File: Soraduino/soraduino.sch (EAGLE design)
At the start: 1 part, among them IC1 ATMEGA168-AU

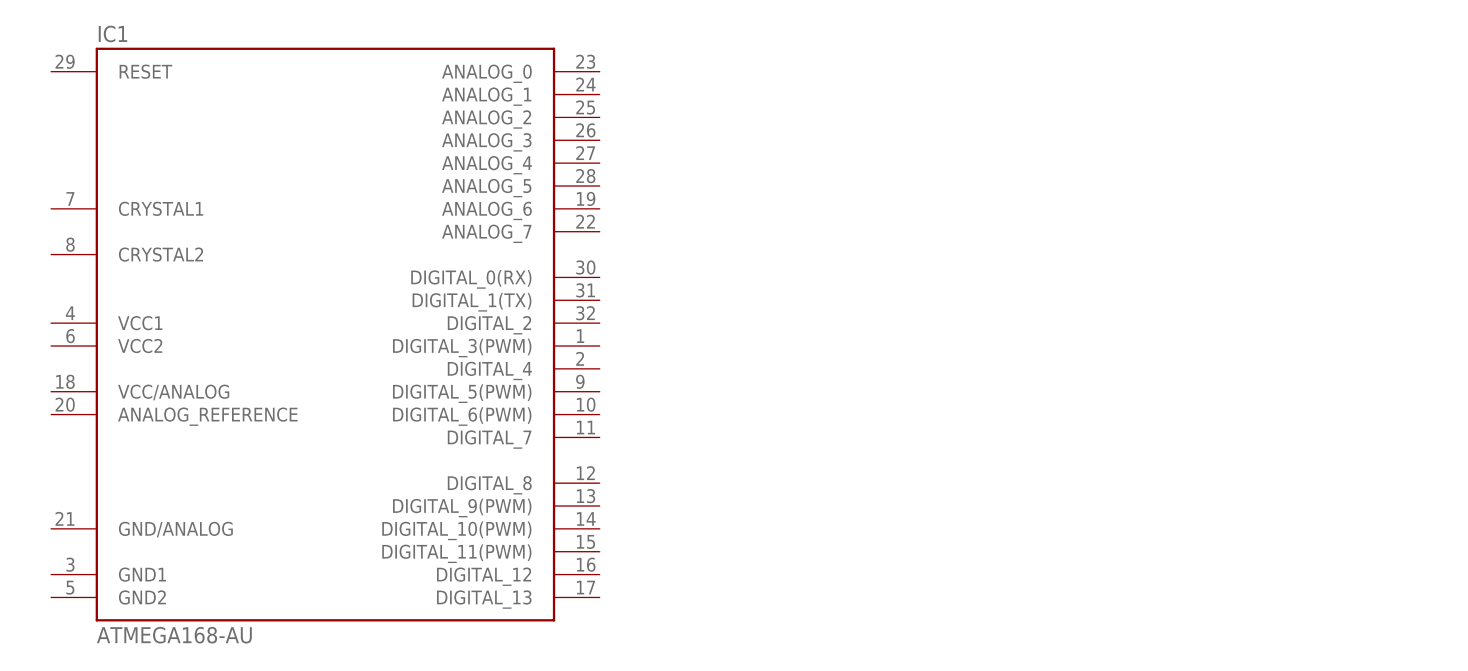
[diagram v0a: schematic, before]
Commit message: crystal設置
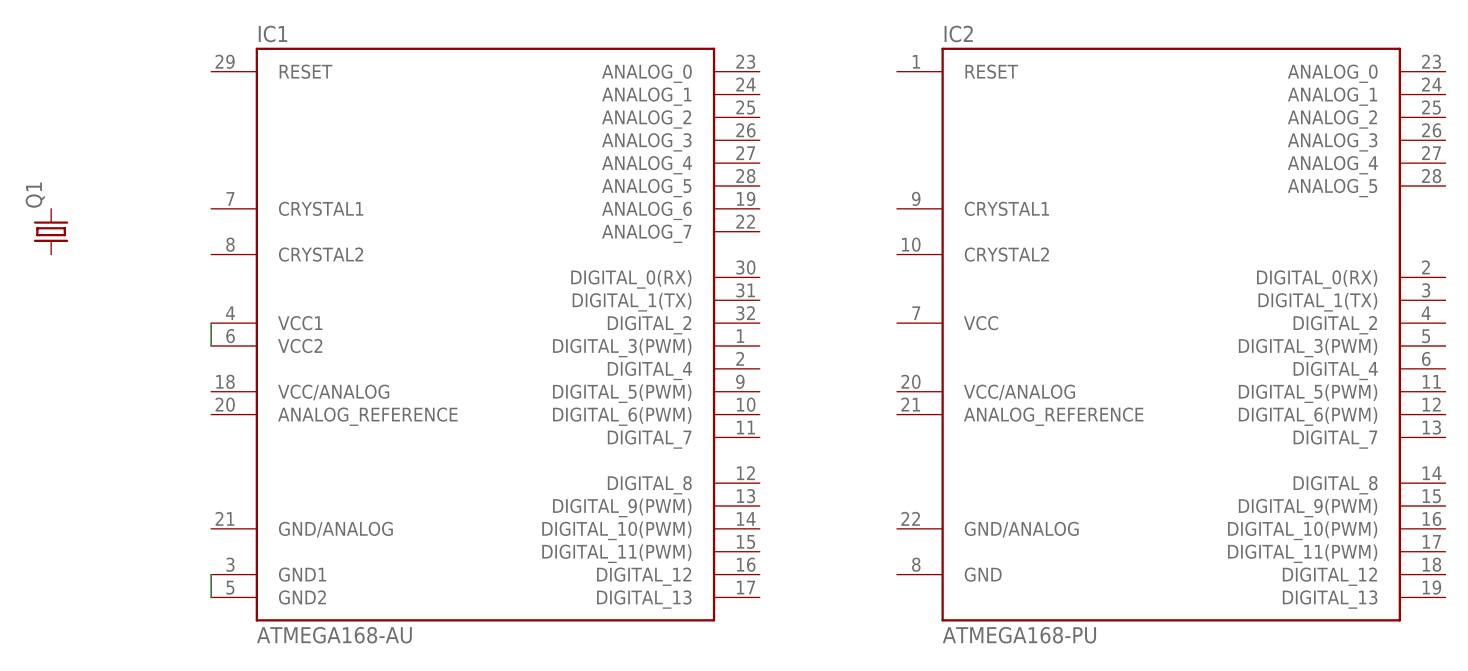
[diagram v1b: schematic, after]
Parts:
- added IC2: ATMEGA168-PU, Arduino-AVR:ATMEGA168-PU
- added Q1: (no value), crystal:CRYSTALHC49S
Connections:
- new net N$1: IC1.VCC1, IC1.VCC2
- new net N$2: IC1.GND1, IC1.GND2
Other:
- moved on the sheet: IC1
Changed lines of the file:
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@@
 <parts>
 <part name="IC1" library="Arduino-AVR" deviceset="ATMEGA168" device="-AU"/>
+<part name="IC2" library="Arduino-AVR" deviceset="ATMEGA168-PU" device=""/>
+<part name="Q1" library="crystal" deviceset="CRYSTAL" device="HC49S"/>
 </parts>
 <sheets>
@@
 </plain>
 <instances>
-<instance part="IC1" gate="1" x="86.36" y="38.1"/>
+<instance part="IC1" gate="1" x="104.14" y="38.1"/>
+<instance part="IC2" gate="1" x="180.34" y="38.1"/>
+<instance part="Q1" gate="G$1" x="55.88" y="48.26" rot="R90"/>
 </instances>
 <busses>
 </busses>
 <nets>
+<net name="N$1" class="0">
+<segment>
+<pinref part="IC1" gate="1" pin="VCC2"/>
+<pinref part="IC1" gate="1" pin="VCC1"/>
+<wire x1="73.66" y1="35.56" x2="73.66" y2="38.1" width="0.1524" layer="91"/>
+</segment>
+</net>
+<net name="N$2" class="0">
+<segment>
+<pinref part="IC1" gate="1" pin="GND2"/>
+<pinref part="IC1" gate="1" pin="GND1"/>
+<wire x1="73.66" y1="7.62" x2="73.66" y2="10.16" width="0.1524" layer="91"/>
+</segment>
+</net>
 </nets>
 </sheet>
